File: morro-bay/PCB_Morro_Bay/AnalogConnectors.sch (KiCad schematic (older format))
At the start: 20 parts, among them J10 Conn_01x04, J11 Conn_01x04, J12 Conn_01x04, J13 Conn_01x04, J14 Conn_01x04, J15 Conn_01x04, J16 Conn_01x04, J17 Conn_01x04, J18 Conn_01x04, J19 Conn_01x04, J20 Conn_01x04, J21 Conn_01x04, J22 Conn_01x04, J3 Conn_01x04, J4 Conn_01x04, J5 Conn_01x04, J6 Conn_01x04, J7 Conn_01x04, J8 Conn_01x04, J9 Conn_01x04

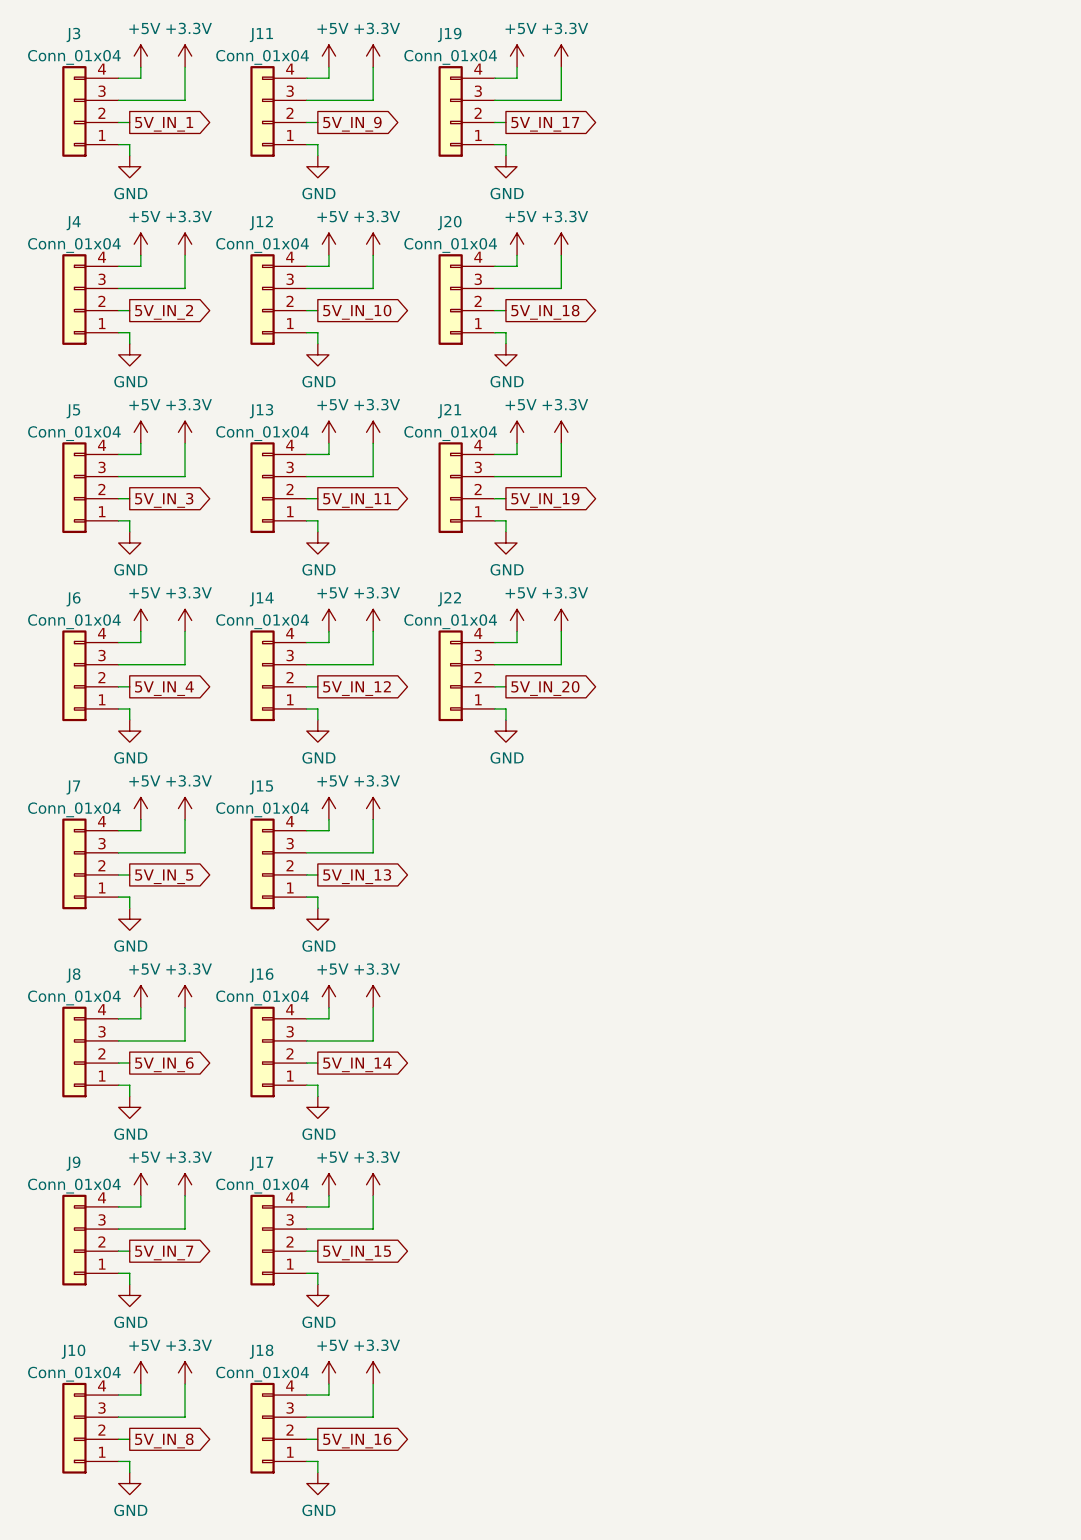
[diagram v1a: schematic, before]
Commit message: External ADC, SPI
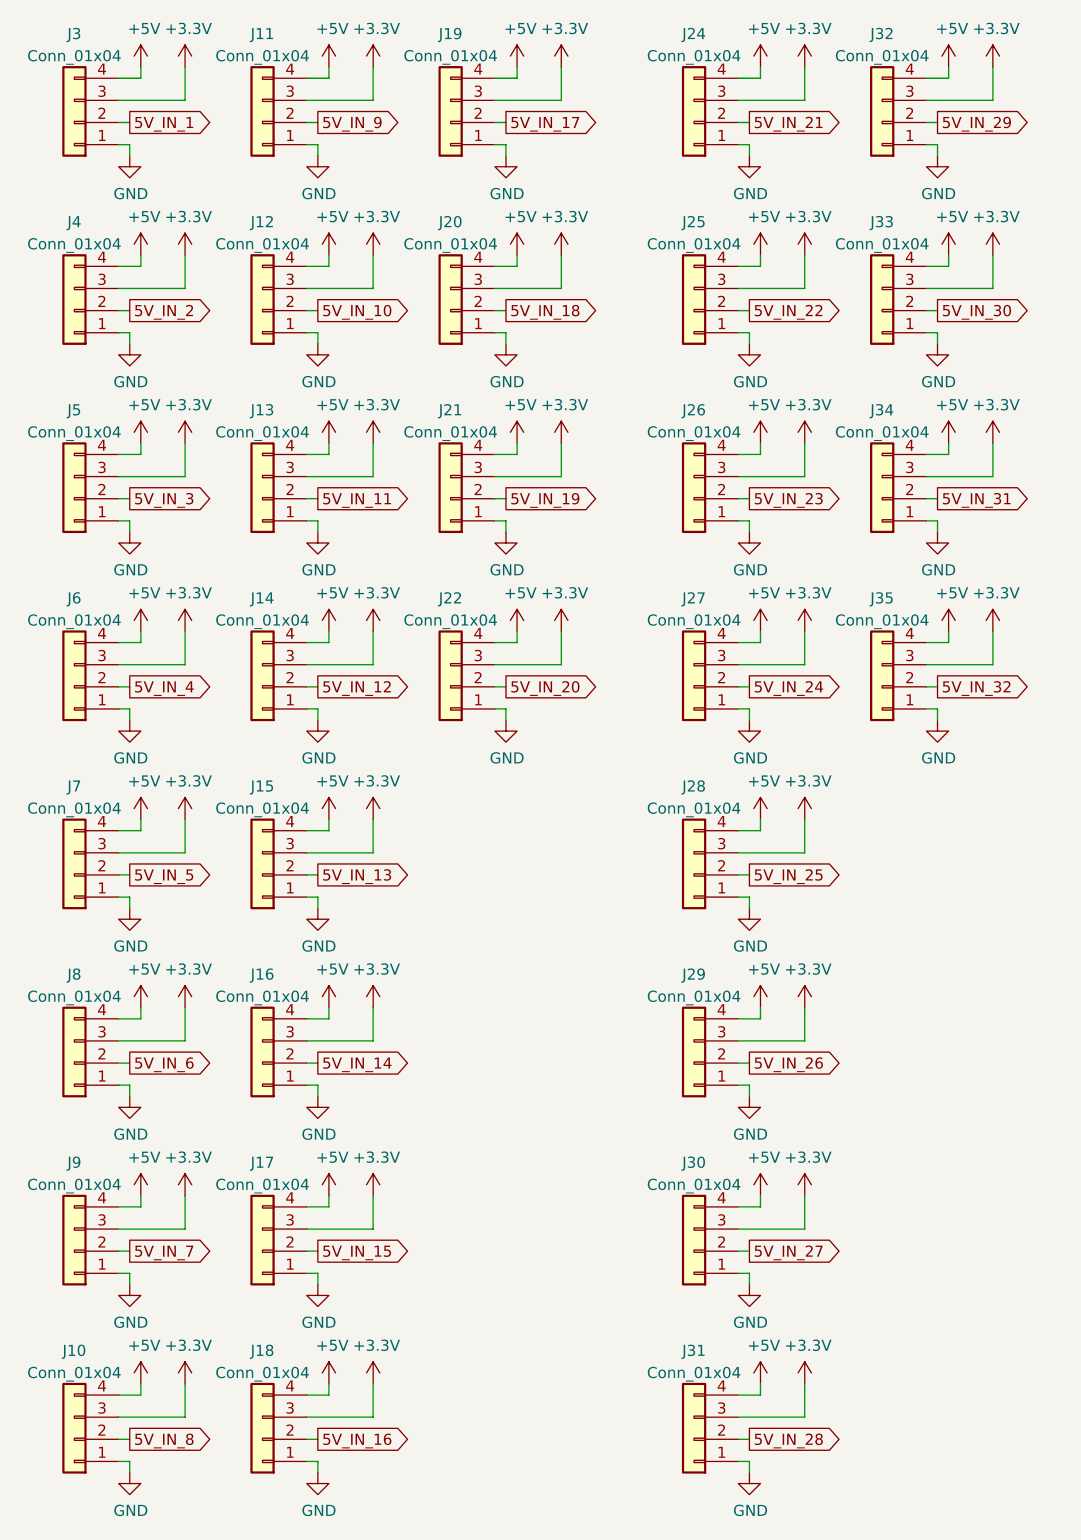
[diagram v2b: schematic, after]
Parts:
- added J24, J25, J26, J27, J28, J29, J30, J31, J32, J33, J34, J35: Conn_01x04, symbol Connector_Generic:Conn_01x04
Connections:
- net +3V3: now also J24.3 (Pin_3), J25.3 (Pin_3), J26.3 (Pin_3), J27.3 (Pin_3), J28.3 (Pin_3), J29.3 (Pin_3), J30.3 (Pin_3), J31.3 (Pin_3), J32.3 (Pin_3), J33.3 (Pin_3), J34.3 (Pin_3), J35.3 (Pin_3)
- net +5V: now also J24.4 (Pin_4), J25.4 (Pin_4), J26.4 (Pin_4), J27.4 (Pin_4), J28.4 (Pin_4), J29.4 (Pin_4), J30.4 (Pin_4), J31.4 (Pin_4), J32.4 (Pin_4), J33.4 (Pin_4), J34.4 (Pin_4), J35.4 (Pin_4)
- net GND: now also J24.1 (Pin_1), J25.1 (Pin_1), J26.1 (Pin_1), J27.1 (Pin_1), J28.1 (Pin_1), J29.1 (Pin_1), J30.1 (Pin_1), J31.1 (Pin_1), J32.1 (Pin_1), J33.1 (Pin_1), J34.1 (Pin_1), J35.1 (Pin_1)
- new net 5V_IN_21: J24.2 (Pin_2)
- new net 5V_IN_22: J25.2 (Pin_2)
- new net 5V_IN_23: J26.2 (Pin_2)
- new net 5V_IN_24: J27.2 (Pin_2)
- new net 5V_IN_25: J28.2 (Pin_2)
- new net 5V_IN_26: J29.2 (Pin_2)
- new net 5V_IN_27: J30.2 (Pin_2)
- new net 5V_IN_28: J31.2 (Pin_2)
- new net 5V_IN_29: J32.2 (Pin_2)
- new net 5V_IN_30: J33.2 (Pin_2)
- new net 5V_IN_31: J34.2 (Pin_2)
- new net 5V_IN_32: J35.2 (Pin_2)

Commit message: More BOM
And if that don't work, use more gun.
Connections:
- net 5V_IN_21 is gone; now on net 5V_IN_13: J24.2 (Pin_2)
- net 5V_IN_22 is gone; now on net 5V_IN_14: J25.2 (Pin_2)
- net 5V_IN_23 is gone; now on net 5V_IN_15: J26.2 (Pin_2)
- net 5V_IN_24 is gone; now on net 5V_IN_16: J27.2 (Pin_2)
- net 5V_IN_15: no longer J17.2 (Pin_2)
- net 5V_IN_16: no longer J18.2 (Pin_2)
- net 5V_IN_17 renamed 10V_IN_3
- net 5V_IN_18 renamed 10V_IN_4
- net 5V_IN_19 renamed 10V_IN_5
- net 5V_IN_20 renamed 10V_IN_6
- net 5V_IN_25 renamed 10V_IN_7
- net 5V_IN_26 renamed 10V_IN_8
- net 5V_IN_27 renamed 10V_IN_9
- net 5V_IN_28 renamed 10V_IN_10
- new net 10V_IN_1: J17.2 (Pin_2)
- new net 10V_IN_2: J18.2 (Pin_2)
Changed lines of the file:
@@
 Wire Wire Line
 	1800 2750 1850 2750
-Text GLabel 1850 2750 2    50   Output ~ 0
-5V_IN_11
 Wire Wire Line
 	1800 3700 1850 3700
@@
 Wire Wire Line
 	1800 3600 1850 3600
-Text GLabel 1850 3600 2    50   Output ~ 0
-5V_IN_12
 Wire Wire Line
 	1800 4550 1850 4550
@@
 Wire Wire Line
 	1800 4450 1850 4450
-Text GLabel 1850 4450 2    50   Output ~ 0
-5V_IN_13
 Wire Wire Line
 	1800 5400 1850 5400
@@
 Wire Wire Line
 	1800 5300 1850 5300
-Text GLabel 1850 5300 2    50   Output ~ 0
-5V_IN_14
 Wire Wire Line
 	1800 6250 1850 6250
@@
 Wire Wire Line
 	1800 6150 1850 6150
-Text GLabel 1850 6150 2    50   Output ~ 0
-5V_IN_15
 Wire Wire Line
 	1800 7100 1850 7100
@@
 Wire Wire Line
 	1800 7000 1850 7000
-Text GLabel 1850 7000 2    50   Output ~ 0
-5V_IN_16
 Wire Wire Line
 	2650 1150 2700 1150
@@
 Wire Wire Line
 	2650 1050 2700 1050
-Text GLabel 2700 1050 2    50   Output ~ 0
-5V_IN_17
 Wire Wire Line
 	2650 2000 2700 2000
@@
 Wire Wire Line
 	2650 1900 2700 1900
-Text GLabel 2700 1900 2    50   Output ~ 0
-5V_IN_18
 Wire Wire Line
 	2650 2850 2700 2850
@@
 Wire Wire Line
 	2650 2750 2700 2750
-Text GLabel 2700 2750 2    50   Output ~ 0
-5V_IN_19
 Wire Wire Line
 	2650 3700 2700 3700
@@
 Wire Wire Line
 	2650 3600 2700 3600
-Text GLabel 2700 3600 2    50   Output ~ 0
-5V_IN_20
 Wire Wire Line
 	3750 1150 3800 1150
@@
 	3750 1050 3800 1050
 Text GLabel 3800 1050 2    50   Output ~ 0
-5V_IN_21
+5V_IN_13
 Wire Wire Line
 	3750 2000 3800 2000
@@
 	3750 1900 3800 1900
 Text GLabel 3800 1900 2    50   Output ~ 0
-5V_IN_22
+5V_IN_14
 Wire Wire Line
 	3750 2850 3800 2850
@@
 	3750 2750 3800 2750
 Text GLabel 3800 2750 2    50   Output ~ 0
-5V_IN_23
+5V_IN_15
 Wire Wire Line
 	3750 3700 3800 3700
@@
 	3750 3600 3800 3600
 Text GLabel 3800 3600 2    50   Output ~ 0
-5V_IN_24
+5V_IN_16
 Wire Wire Line
 	3750 4550 3800 4550
@@
 Wire Wire Line
 	3750 4450 3800 4450
-Text GLabel 3800 4450 2    50   Output ~ 0
-5V_IN_25
 Wire Wire Line
 	3750 5400 3800 5400
@@
 Wire Wire Line
 	3750 5300 3800 5300
-Text GLabel 3800 5300 2    50   Output ~ 0
-5V_IN_26
 Wire Wire Line
 	3750 6250 3800 6250
@@
 Wire Wire Line
 	3750 6150 3800 6150
-Text GLabel 3800 6150 2    50   Output ~ 0
-5V_IN_27
 Wire Wire Line
 	3750 7100 3800 7100
@@
 Wire Wire Line
 	3750 7000 3800 7000
-Text GLabel 3800 7000 2    50   Output ~ 0
-5V_IN_28
 Wire Wire Line
 	4600 1150 4650 1150
@@
 Text GLabel 4650 3600 2    50   Output ~ 0
 5V_IN_32
+Text GLabel 1850 6150 2    50   Output ~ 0
+10V_IN_1
+Text GLabel 1850 7000 2    50   Output ~ 0
+10V_IN_2
+Text GLabel 2700 1050 2    50   Output ~ 0
+10V_IN_3
+Text GLabel 2700 1900 2    50   Output ~ 0
+10V_IN_4
+Text GLabel 2700 2750 2    50   Output ~ 0
+10V_IN_5
+Text GLabel 2700 3600 2    50   Output ~ 0
+10V_IN_6
+Text GLabel 1850 2750 2    50   Output ~ 0
+5V_IN_11
+Text GLabel 1850 3600 2    50   Output ~ 0
+5V_IN_12
+Text GLabel 1850 4450 2    50   Output ~ 0
+5V_IN_13
+Text GLabel 1850 5300 2    50   Output ~ 0
+5V_IN_14
+Text GLabel 3800 4450 2    50   Output ~ 0
+10V_IN_7
+Text GLabel 3800 5300 2    50   Output ~ 0
+10V_IN_8
+Text GLabel 3800 6150 2    50   Output ~ 0
+10V_IN_9
+Text GLabel 3800 7000 2    50   Output ~ 0
+10V_IN_10
 $EndSCHEMATC

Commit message: BOM BOM BOM BOM baBOM BOM baBOM...
(Imperial march)
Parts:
- removed J32, J33, J34, J35: Conn_01x04, symbol Connector_Generic:Conn_01x04
- J3: Digikey (none) -> https://www.digikey.ca/product-detail/en/molex/0705510038/W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; Part Number (none) -> 0705510038
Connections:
- net 5V_IN_13: no longer J24.2 (Pin_2)
- net 5V_IN_14: no longer J25.2 (Pin_2)
- net 5V_IN_15: now also J24.2 (Pin_2); no longer J26.2 (Pin_2)
- net 5V_IN_16: now also J25.2 (Pin_2); no longer J27.2 (Pin_2)
- new net 5V_IN_17: J26.2 (Pin_2)
- new net 5V_IN_18: J27.2 (Pin_2)

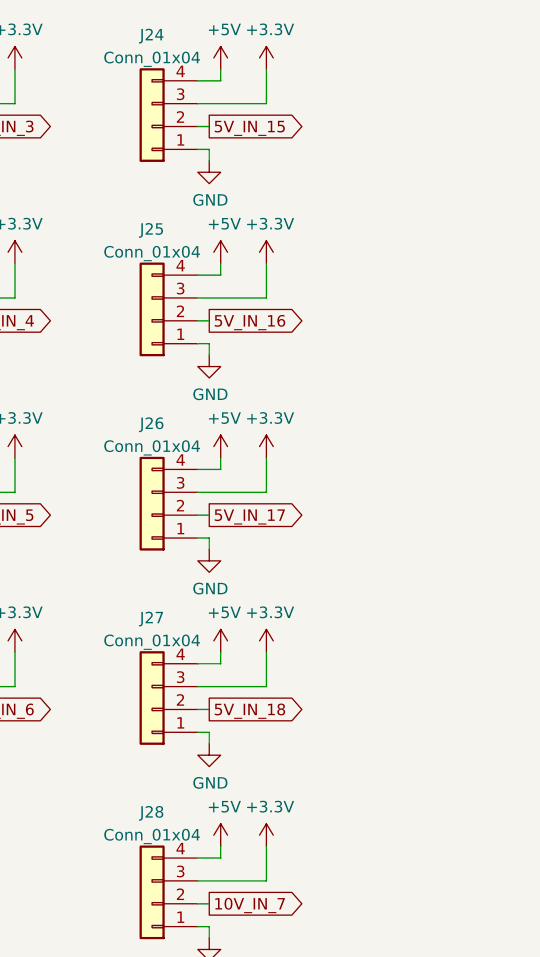
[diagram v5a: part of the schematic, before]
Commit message: Start layout, finish BOM
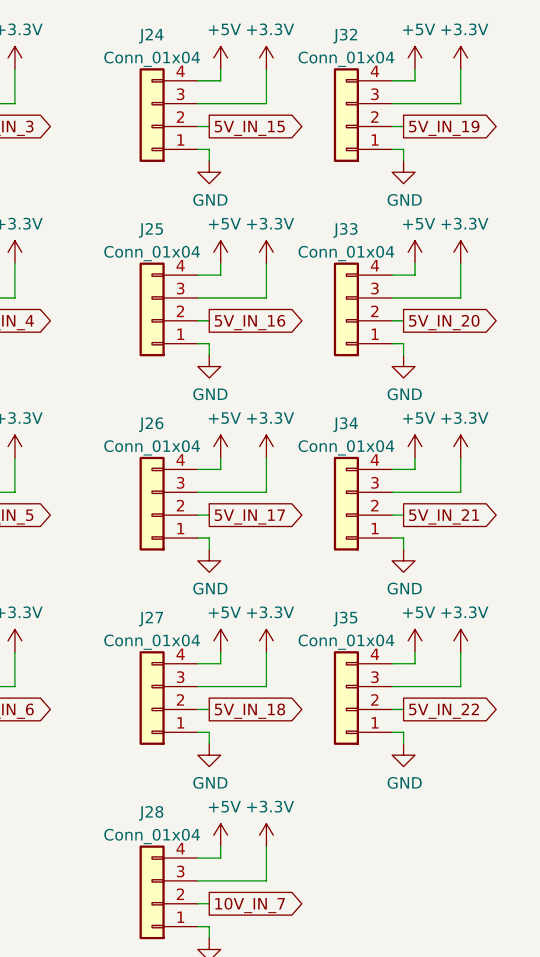
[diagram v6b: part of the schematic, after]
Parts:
- added J32, J33, J34, J35: Conn_01x04, PCB_Morro_Bay:Connector_Molex_SL_4POS_0705510038, symbol Connector_Generic:Conn_01x04
- J10, J11, J12, J13, J14, J15, J16, J17, J18, J19, J20, J21, J22, J24, J25, J26, J27, J28, J29, J30, J31, J4, J5, J6, J7, J8, J9: footprint (none) -> PCB_Morro_Bay:Connector_Molex_SL_4POS_0705510038; Digikey (none) -> https://www.digikey.ca/product-detail/en/molex/0705510038/W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; Part Number (none) -> 0705510038
- J3: footprint (none) -> PCB_Morro_Bay:Connector_Molex_SL_4POS_0705510038
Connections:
- net +3V3: now also J32.3 (Pin_3), J33.3 (Pin_3), J34.3 (Pin_3), J35.3 (Pin_3)
- net +5V: now also J32.4 (Pin_4), J33.4 (Pin_4), J34.4 (Pin_4), J35.4 (Pin_4)
- net GND: now also J32.1 (Pin_1), J33.1 (Pin_1), J34.1 (Pin_1), J35.1 (Pin_1)
- new net 5V_IN_19: J32.2 (Pin_2)
- new net 5V_IN_20: J33.2 (Pin_2)
- new net 5V_IN_21: J34.2 (Pin_2)
- new net 5V_IN_22: J35.2 (Pin_2)
